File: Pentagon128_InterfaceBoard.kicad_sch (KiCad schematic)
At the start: 36 parts, among them J1 DIN41612_02x32_AB, J10 Tape Out, J11 Tape In, J12 Mini-DIN-6, J13 Conn_02x05_Odd_Even ATmega Pr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, J14 Barrel_Jack_Switch, J2 Conn_02x03_Odd_Even ATmega Pr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, J3 Conn_02x08_Odd_Even Ext Keyb, J4 Conn_02x05_Odd_Even Kempston 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, J5 DE9_Plug Kempston Out SMD, J6 DE15_Plug_HighDensity VGA CRT, J7 Conn_01x04 FDD Power, J8 Conn_01x04 Audio In, J9 AudioJack3, Q1 Q_NPN_BCE, Q2 Q_NPN_BCE, Q3 Q_NPN_BCE, Q4 Q_NPN_BCE, U1 MT8816 PLCC44, U2 ATmega168PA-A

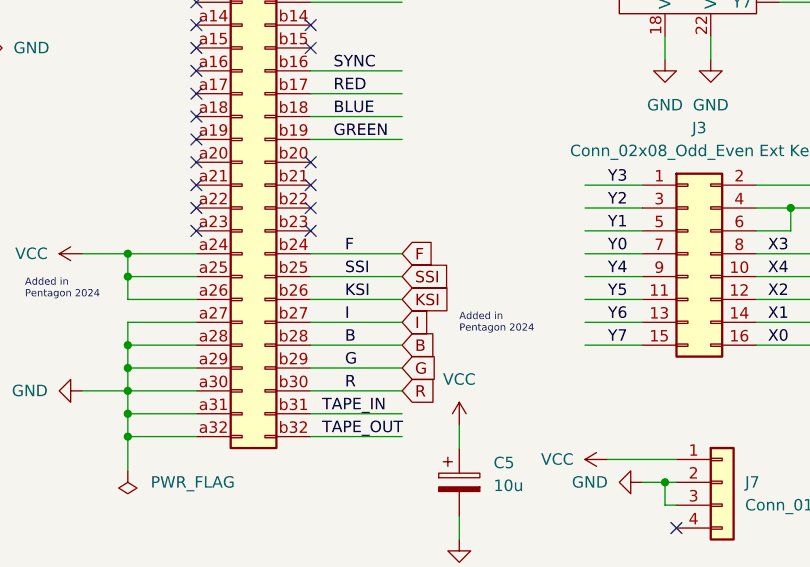
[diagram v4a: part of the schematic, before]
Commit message: Add missing pico_RGB_TO_VGA.kicad_sch. Add 1 dummy pin to RGBI connector. Rename KSI -> KS, SSI -> SS.
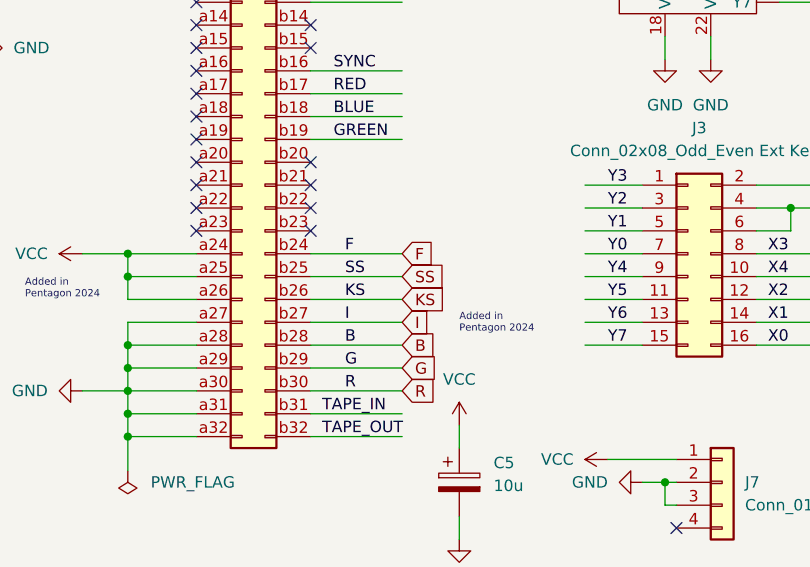
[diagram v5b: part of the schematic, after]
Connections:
- net KSI renamed KS
- net SSI renamed SS
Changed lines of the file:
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@@
     (effects (font (size 1.27 1.27)) (justify left bottom))
   )
-  (label "KSI" (at 217.17 132.08 0) (fields_autoplaced)
+  (label "KS" (at 217.17 132.08 0) (fields_autoplaced)
     (effects (font (size 1.27 1.27)) (justify left bottom))
   )
@@
     (effects (font (size 1.27 1.27)) (justify left bottom))
   )
-  (label "SSI" (at 217.17 129.54 0) (fields_autoplaced)
+  (label "SS" (at 217.17 129.54 0) (fields_autoplaced)
     (effects (font (size 1.27 1.27)) (justify left bottom))
   )
@@
     )
   )
-  (global_label "KSI" (shape input) (at 223.52 132.08 0) (fields_autoplaced)
-    (effects (font (size 1.27 1.27)) (justify left))
-    (property "Intersheetrefs" "${INTERSHEET_REFS}" (at 229.5895 132.08 0)
+  (global_label "KS" (shape input) (at 223.52 132.08 0) (fields_autoplaced)
+    (effects (font (size 1.27 1.27)) (justify left))
+    (property "Intersheetrefs" "${INTERSHEET_REFS}" (at 228.9847 132.08 0)
       (effects (font (size 1.27 1.27)) (justify left) hide)
     )
@@
     )
   )
-  (global_label "SSI" (shape input) (at 223.52 129.54 0) (fields_autoplaced)
-    (effects (font (size 1.27 1.27)) (justify left))
-    (property "Intersheetrefs" "${INTERSHEET_REFS}" (at 229.529 129.54 0)
-      (effects (font (size 1.27 1.27)) (justify left) hide)
-    )
+  (global_label "SS" (shape input) (at 223.52 129.54 0) (fields_autoplaced)
+    (effects (font (size 1.27 1.27)) (justify left))
+    (property "Intersheetrefs" "${INTERSHEET_REFS}" (at 228.9242 129.54 0)
+      (effects (font (size 1.27 1.27)) (justify left) hide)
+    )
